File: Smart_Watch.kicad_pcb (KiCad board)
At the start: 4 copper layers, 32.6 x 32.6 mm, 77 parts, among them J2 Conn_01x02, J3 Conn_01x06, J4 Conn_01x02, J7 USB4110GFA, SW2 SW_Push, SW3 SW_Push, SW4 SW_Push, SW5 SW_Push, SW6 SW_Push, SW7 SW_Push, U1 BMI270, U12 DRV2603RUNR, U2 OPT3004DNPR, U3 NORA-B106-00B, U4 LPS22DF, U5 W25Q32JVSS, U6 NPM1300-QEAA-R7, U7 FAN5622SX, U8 ESDR0502NMUTBG, U9 MAX30102EFD_T, X1 Q13FC1350000400, X608 Display

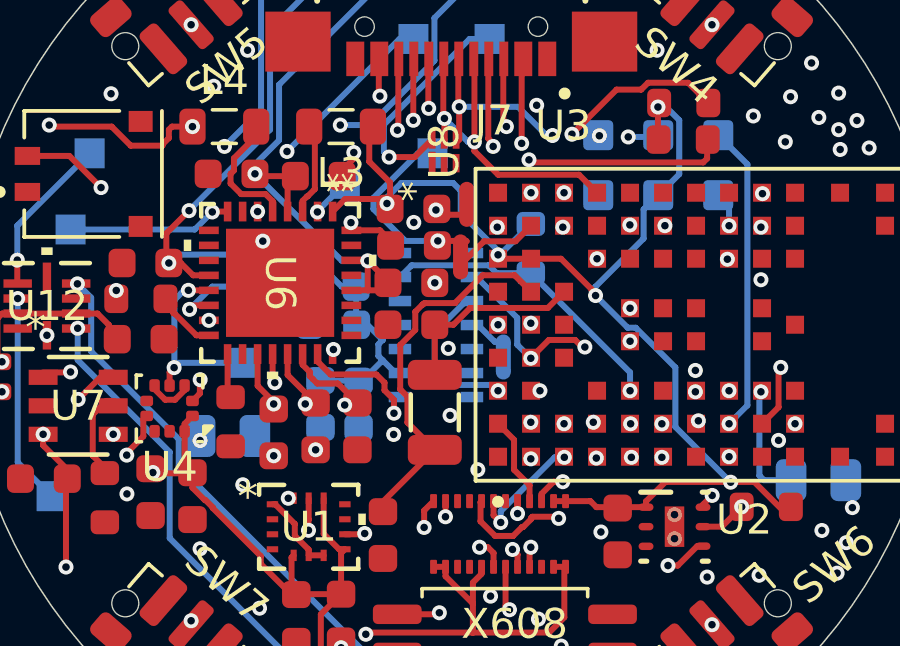
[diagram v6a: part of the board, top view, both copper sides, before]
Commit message: New Case Files + Updated DRC Errors
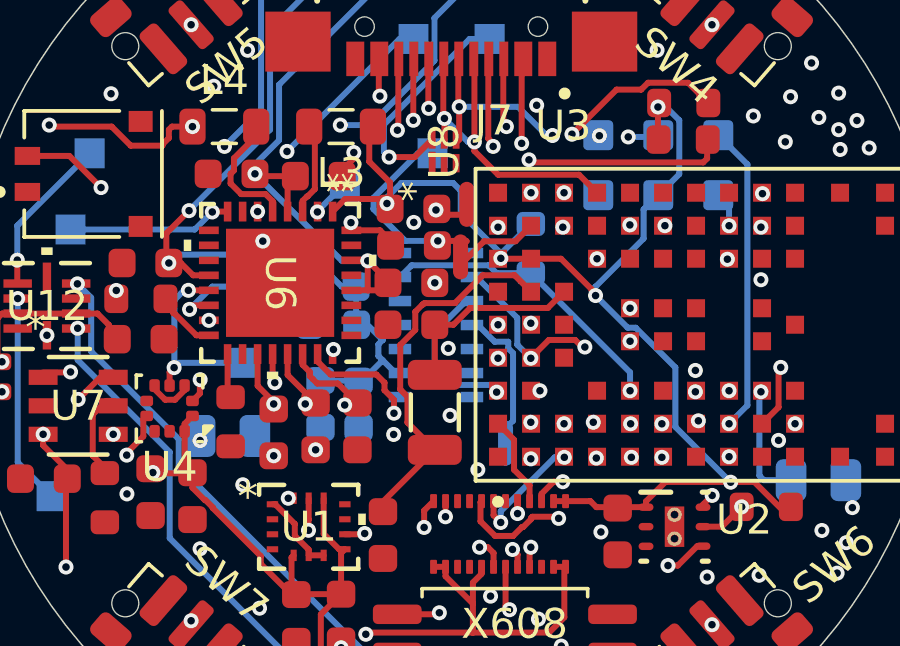
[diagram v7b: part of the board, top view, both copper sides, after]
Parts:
- moved NT3 2.88 mm to (173.9, 111.8)
- moved G*** 1.19 mm to (168.3, 117.6)
- moved G*** 0.08 mm to (181.1, 99.9)
- renumbered TP11 to +1V8, TP10 to +3V0, TP7 to +BATT1, TP14 to GND1, TP1 to LRA_EN1, TP2 to LRA_PWM1, TP15 to PGND1, TP16 to PGND2, TP13 to PMIC_INT1, TP3 to QSPI_CLK1, TP4 to QSPI_CS1, TP6 to SCL1, TP5 to SDA1, TP8 to VBUS_IN1, TP9 to VBUS_OUT1, TP12 to VSYS1
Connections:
- U3 pad A4: unconnected-(U3-P1.00-PadA4) -> /Architecture/MCU/BTN_3
- U3 pad A8: /Architecture/MCU/BTN_3 -> +1V8
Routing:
- net /Architecture/MCU/BTN_3: track 21.0 -> 16.8 mm
- net PGND3: track 1.28 -> 4.49 mm
- net +1V8: track 109.8 -> 110.9 mm, vias 8 -> 9

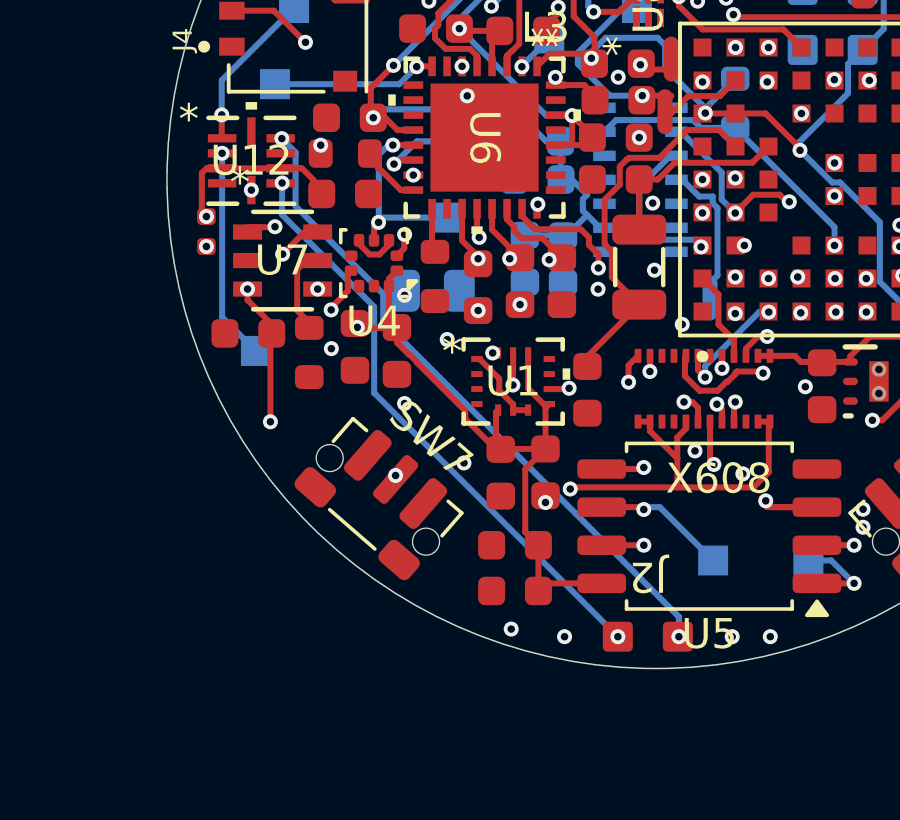
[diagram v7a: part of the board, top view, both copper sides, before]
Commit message: Replaced unavailable JLC components
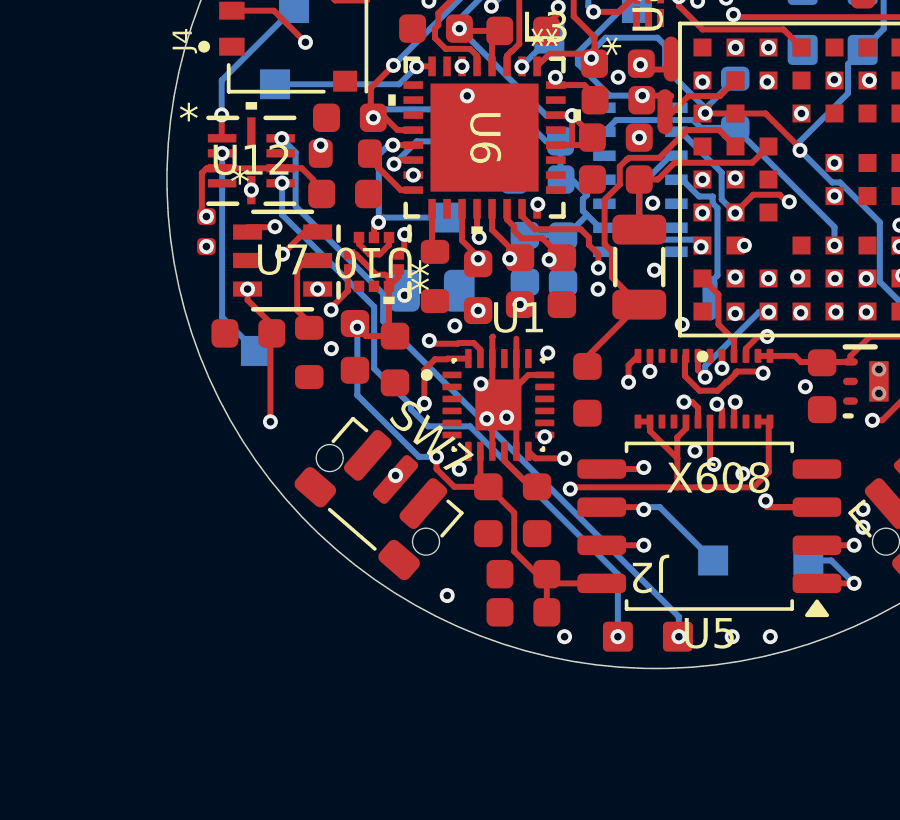
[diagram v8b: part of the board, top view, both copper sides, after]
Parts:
- removed U4: LPS22DF, Package_LGA:ST_HLGA-10_2x2mm_P0.5mm_LayoutBorder3x2y
- added U10: LPS22HHTR, Smart_Watch:HLGA-10L_2X2X0P73_STM-L, F.Cu at (162.7, 110.6)
- U1: value BMI270 -> MPU-6500; footprint Smart_Watch:BMI270_BOS-L -> Smart_Watch:QFN40P300X300X95-25N
- moved C6 2.29 mm to (166.6, 118.9)
- moved C5 1.74 mm to (168.2, 118.9)
- moved C26 1.00 mm to (167.7, 121.0)
- moved U1 0.92 mm to (166.9, 115.4)
- moved C21 0.76 mm to (167.7, 122.3)
- moved C9 0.29 mm to (163.4, 113.8)
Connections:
- C5 pad 1: +1V8 -> Net-(U1-REGOUT)
- U1 pad 1: GND -> (no net)
- U1 pad 10: unconnected-(U1-OCSB-Pad10) -> Net-(U1-REGOUT)
- U1 pad 11: unconnected-(U1-OSDO-Pad11) -> GND
- U1 pad 12: +1V8 -> /Architecture/MCU/BMI_INT
- U1 pad 13: /Architecture/MCU/SCL -> +1V8
- U1 pad 14: /Architecture/MCU/SDA -> (no net)
- U1 pad 2: unconnected-(U1-ASDX-Pad2) -> (no net)
- U1 pad 3: unconnected-(U1-ASCX-Pad3) -> (no net)
- U1 pad 4: unconnected-(U1-INT1-Pad4) -> (no net)
- U1 pad 5: +1V8 -> (no net)
- U1 pad 6: GND -> (no net)
- U1 pad 7: GND -> unconnected-(U1-AUX_CL-Pad7)
- U1 pad 9: /Architecture/MCU/BMI_INT -> GND
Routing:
- net GND: track 8.61 -> 15.8 mm, vias 36 -> 39
- net +1V8: track 110.9 -> 114.1 mm, vias 9 -> 11
- net /Architecture/MCU/BMI_INT: track 17.1 -> 20.1 mm
- net Net-(U1-REGOUT): track 0.00 -> 1.77 mm
- net /Architecture/MCU/SCL: track 61.8 -> 63.1 mm, vias 9 -> 8
- net /Architecture/Peripherals/MOTOR-: track 19.8 -> 20.6 mm
- net /Architecture/MCU/SDA: track 74.8 -> 75.6 mm
- net /Architecture/MCU/BTN_4: track 30.5 -> 31.2 mm
